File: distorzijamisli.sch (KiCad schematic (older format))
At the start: 73 parts, among them J1 SW DBG, J2 USB_OTG, J3 Conn_02x16_Odd_Even, J4 Conn_02x16_Odd_Even, J5 Conn_02x12_Odd_Even, J6 Conn_02x03_Odd_Even, J7 Conn_02x03_Odd_Even, SW1 SW_Push, U1 STM32F407VGTx, X1 Crystal

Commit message: Add codec subsheet
This adds the subsheet with the CS4245 audio codec
connected to the main processor.
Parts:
- removed R16, R22: R_Small, symbol R_Small
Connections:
- net labels added: PB14, PC12
- net labels removed: I2S2_ext_SD, I2S3_ext_SD
- wire segments 372 -> 345
- no-connect marks 16 -> 9

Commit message: Add power regulators with 5, 3 and 3.3V.
In addition, the connector is now as short as needed.
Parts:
- removed J5: Conn_02x12_Odd_Even, symbol Conn_02x12_Odd_Even
- added C55, C58, C60, C63, C65: 1uF, symbol C
- added C56, C59, C61, C64, C66: 100nF, symbol C
- added C57, C62: 10nF, symbol C
- added J12: 5V, symbol Jack-DC
- added J5: Conn_02x08_Odd_Even, symbol Conn_02x08_Odd_Even
- added U3: LD3985M30R_SOT23, TO_SOT_Packages_SMD:SOT-23-5, symbol LD3985M30R_SOT23
- added U4: LD3985M33R_SOT23, TO_SOT_Packages_SMD:SOT-23-5, symbol LD3985M33R_SOT23
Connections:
- net labels added: 3.3V, 3V, 5V
- net labels removed: VCC
- wire segments 345 -> 368
- no-connect marks 9 -> 5

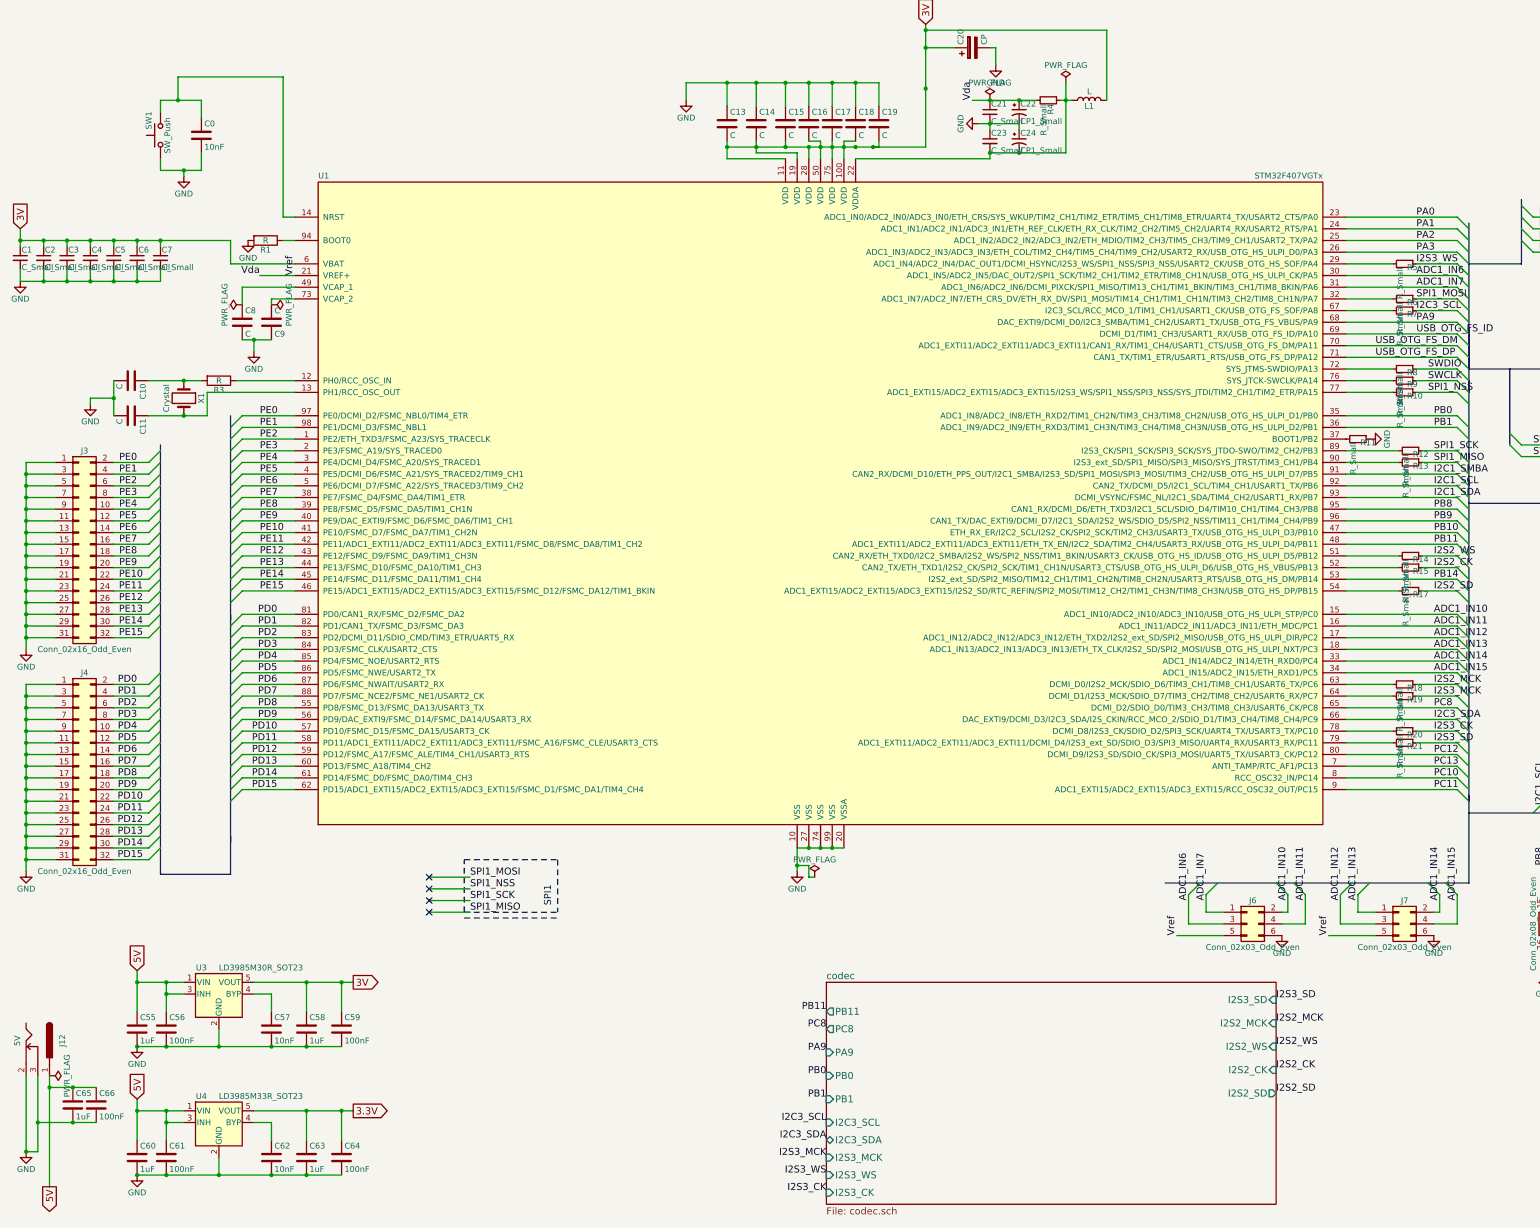
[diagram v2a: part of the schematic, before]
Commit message: Move the I2S2_SD termination resistor to driver
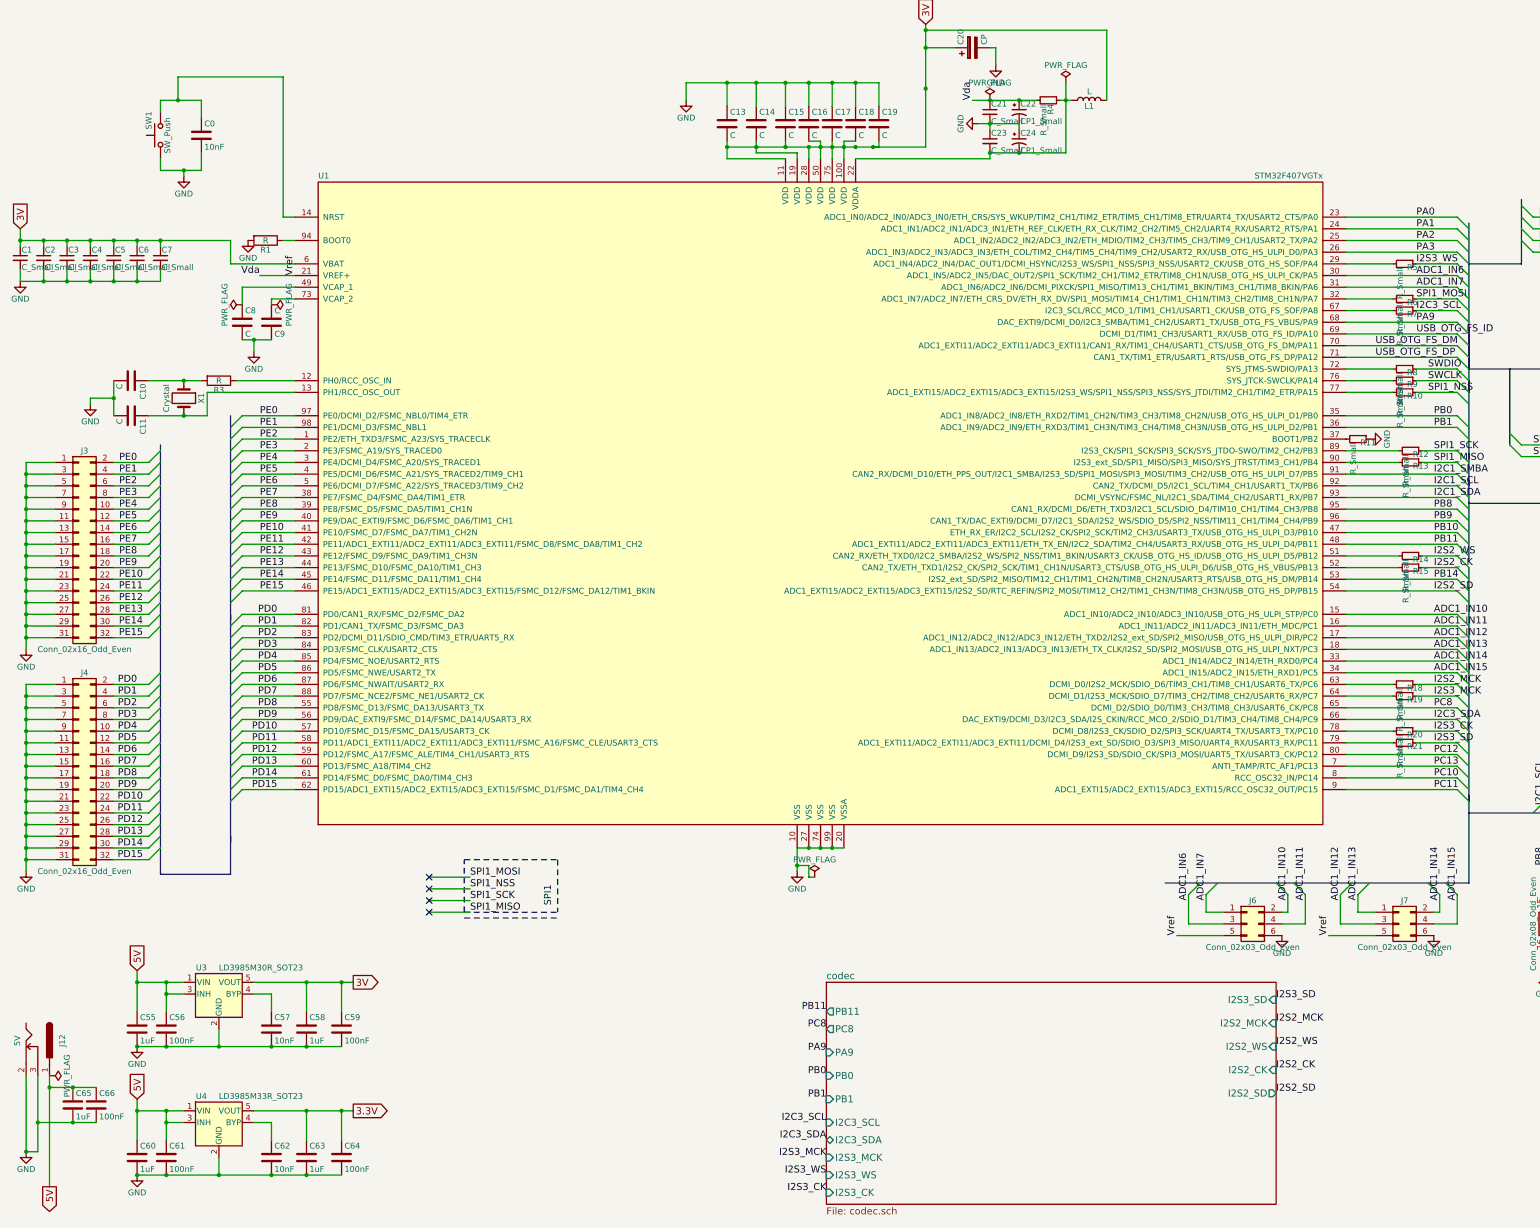
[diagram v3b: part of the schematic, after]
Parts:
- removed R17: R_Small, symbol R_Small
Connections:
- net I2S2_SD: now also U1.54 (ADC1_EXTI15/ADC2_EXTI15/ADC3_EXTI15/I2S2_SD/RTC_REFIN/SPI2_MOSI/TIM12_CH2/TIM1_CH3N/TIM8_CH3N/USB_OTG_HS_DP/PB15)

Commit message: Set values to components and minor fixes.
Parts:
- removed C20: CP, symbol CP
- added C20: 1uF, symbol C
- added R16, R2: 0, symbol R
- added R17: 100k, symbol R
- added R22: 220, symbol R
- C0: value 10nF -> 100nF
- C1, C2, C21, C23, C3, C4, C5, C6: value C_Small -> 100n
- C10, C11: value C -> 20pF
- C13, C14, C15, C16, C17, C18, C19: value C -> 100n
- C22, C24: value CP1_Small -> 1uF
- C7: value C_Small -> 1u
- C8, C9: value C -> 2.2u
- L1: value L -> fcm1608-0603
- R1: value R -> 100k
- R10, R11, R12, R13, R14, R15, R18, R19, R20, R21, R5, R6, R7: value R_Small -> 0
- R23, R24, R25, R26: value R_Small -> 1k
- R27: value R -> 1k5
- R28, R29, R3, R30: value R -> 0
- R31, R32, R33, R34, R35: value R_Small -> 10k
- R4: value R_Small -> 47
- R8, R9: value R_Small -> 22
- X1: value Crystal -> 8MHz
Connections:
- net 3V: now also R31.1, R32.1, R33.1, R34.1, R35.1, C20.2, R17.2, R2.2; no longer C1.1, C2.1, C3.1, C4.1, C5.1, C6.1, C7.1, U1.6 (VBAT)
- net GND: now also C24.2, C20.1; no longer C24.1
- net at C11.1, X1.2: now also R22.2; no longer U1.13 (PH1/RCC_OSC_OUT)
- net at C0.1, SW1.2, U1.14 (NRST): now also R17.1
- net at C23.2, L1.1, R4.1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: now also C24.1; no longer C24.2
- new net: R22.1, U1.13 (PH1/RCC_OSC_OUT)
- new net: R16.1, U1.6 (VBAT)
- new net: C1.1, C2.1, C3.1, C4.1, C5.1, C6.1, C7.1, R16.2, R2.1
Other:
- moved on the sheet: R3

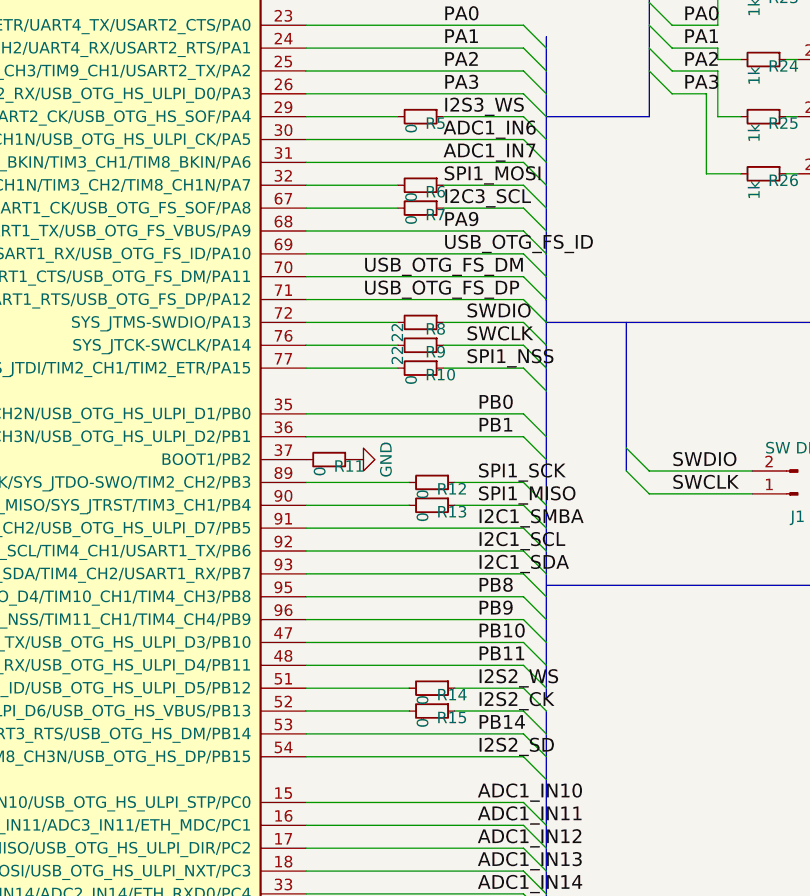
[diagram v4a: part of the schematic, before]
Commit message: Termination resistors
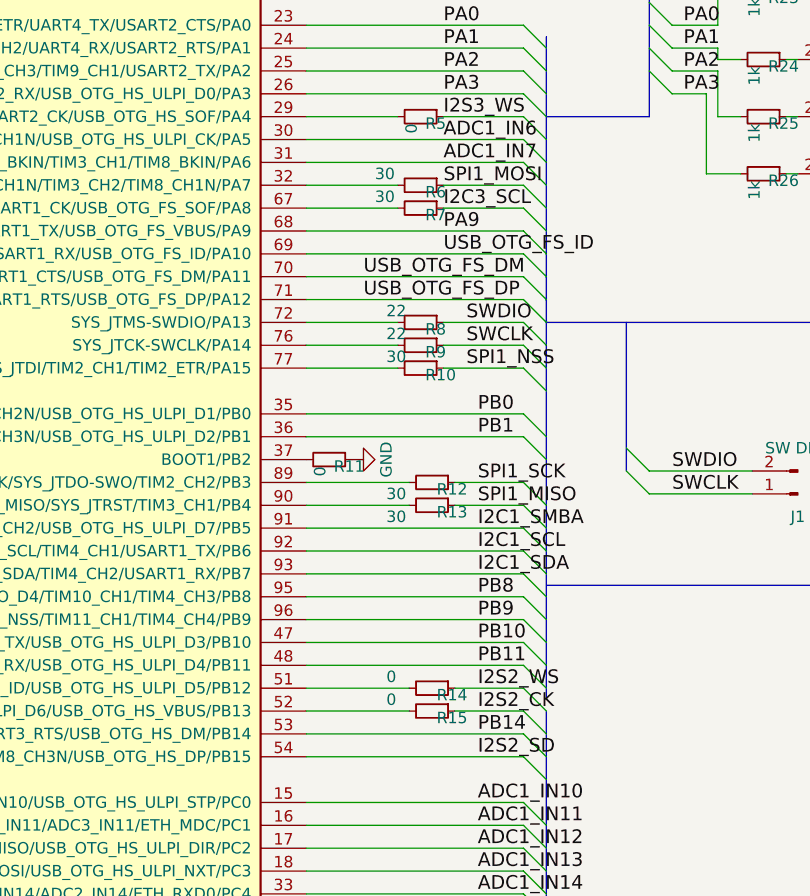
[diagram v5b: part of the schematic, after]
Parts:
- R10, R12, R13, R6, R7: value 0 -> 30
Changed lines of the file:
@@
 P 12500 3250
 F 0 "R6" V 12530 3270 50  0000 L CNN
-F 1 "0" H 12530 3210 50  0000 L CNN
+F 1 "30" V 12450 3050 50  0000 L CNN
 F 2 "" H 12500 3250 50  0001 C CNN
 F 3 "" H 12500 3250 50  0001 C CNN
@@
 P 12500 3350
 F 0 "R7" V 12530 3370 50  0000 L CNN
-F 1 "0" H 12530 3310 50  0000 L CNN
+F 1 "30" V 12450 3150 50  0000 L CNN
 F 2 "" H 12500 3350 50  0001 C CNN
 F 3 "" H 12500 3350 50  0001 C CNN
@@
 P 12500 3850
 F 0 "R8" V 12530 3870 50  0000 L CNN
-F 1 "22" H 12500 3750 50  0000 L CNN
+F 1 "22" V 12450 3700 50  0000 L CNN
 F 2 "" H 12500 3850 50  0001 C CNN
 F 3 "" H 12500 3850 50  0001 C CNN
@@
 P 12500 3950
 F 0 "R9" V 12530 3970 50  0000 L CNN
-F 1 "22" H 12500 3850 50  0000 L CNN
+F 1 "22" V 12450 3800 50  0000 L CNN
 F 2 "" H 12500 3950 50  0001 C CNN
 F 3 "" H 12500 3950 50  0001 C CNN
@@
 P 12500 4050
 F 0 "R10" V 12530 4070 50  0000 L CNN
-F 1 "0" H 12530 4010 50  0000 L CNN
+F 1 "30" V 12450 3900 50  0000 L CNN
 F 2 "" H 12500 4050 50  0001 C CNN
 F 3 "" H 12500 4050 50  0001 C CNN
@@
 P 12550 4550
 F 0 "R12" V 12580 4570 50  0000 L CNN
-F 1 "0" H 12580 4510 50  0000 L CNN
+F 1 "30" V 12600 4350 50  0000 L CNN
 F 2 "" H 12550 4550 50  0001 C CNN
 F 3 "" H 12550 4550 50  0001 C CNN
@@
 P 12550 4650
 F 0 "R13" V 12580 4670 50  0000 L CNN
-F 1 "0" H 12580 4610 50  0000 L CNN
+F 1 "30" V 12600 4450 50  0000 L CNN
 F 2 "" H 12550 4650 50  0001 C CNN
 F 3 "" H 12550 4650 50  0001 C CNN
@@
 P 12550 5450
 F 0 "R14" V 12580 5470 50  0000 L CNN
-F 1 "0" H 12580 5410 50  0000 L CNN
+F 1 "0" V 12500 5250 50  0000 L CNN
 F 2 "" H 12550 5450 50  0001 C CNN
 F 3 "" H 12550 5450 50  0001 C CNN
@@
 P 12550 5550
 F 0 "R15" V 12580 5570 50  0000 L CNN
-F 1 "0" H 12580 5510 50  0000 L CNN
+F 1 "0" V 12500 5350 50  0000 L CNN
 F 2 "" H 12550 5550 50  0001 C CNN
 F 3 "" H 12550 5550 50  0001 C CNN

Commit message: Add some of the pinouts
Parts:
- C0, L1: footprint (none) -> Inductors_SMD:L_0603_HandSoldering
- J1: footprint (none) -> Pin_Headers:Pin_Header_Straight_1x02
- J12: footprint (none) -> Connectors:BARREL_JACK
- J2: footprint (none) -> Connectors:USB_Mini-B
- J3, J4: footprint (none) -> Pin_Headers:Pin_Header_Straight_2x16
- J5: footprint (none) -> Pin_Headers:Pin_Header_Straight_2x08
- J6, J7: footprint (none) -> Pin_Headers:Pin_Header_Straight_2x03
- SW1: footprint (none) -> Buttons_Switches_THT:SW_PUSH_6mm
- U1: footprint LQFP100 -> Housings_QFP:LQFP-100_14x14mm_Pitch0.5mm
- U3, U4: footprint TO_SOT_Packages_SMD:SOT-23-5 -> TO_SOT_Packages_SMD:SOT-23-5_HandSoldering
- X1: footprint (none) -> Crystals:HC-49V
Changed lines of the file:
@@
 F 0 "C0" H 2225 1950 50  0000 L CNN
 F 1 "100nF" H 2225 1750 50  0000 L CNN
-F 2 "" H 2238 1700 50  0001 C CNN
+F 2 "Inductors_SMD:L_0603_HandSoldering" H 2238 1700 50  0001 C CNN
 F 3 "" H 2200 1850 50  0001 C CNN
 	1    2200 1850
@@
 F 0 "SW1" H 1900 1950 50  0000 L CNN
 F 1 "SW_Push" H 1850 1790 50  0000 C CNN
-F 2 "" H 1850 2050 50  0001 C CNN
+F 2 "Buttons_Switches_THT:SW_PUSH_6mm" H 1850 2050 50  0001 C CNN
 F 3 "" H 1850 2050 50  0001 C CNN
 	1    1850 1850
@@
 F 0 "J1" H 14150 4700 50  0000 C CNN
 F 1 "SW DBG" H 14150 4400 50  0000 C CNN
-F 2 "" H 14150 4600 50  0001 C CNN
+F 2 "Pin_Headers:Pin_Header_Straight_1x02" H 14150 4600 50  0001 C CNN
 F 3 "" H 14150 4600 50  0001 C CNN
 	1    14150 4600
@@
 F 0 "X1" H 2050 4250 50  0000 C CNN
 F 1 "8MHz" H 2050 3950 50  0000 C CNN
-F 2 "" H 2050 4100 50  0001 C CNN
-F 3 "" H 2050 4100 50  0001 C CNN
+F 2 "Crystals:HC-49V" H 2050 4100 50  0001 C CNN
+F 3 "CX49GFNB08000H0PESZZ" H 2050 4100 50  0001 C CNN
 	1    2050 4100
 	0    1    1    0
@@
 F 0 "J2" H 15450 4500 50  0000 L CNN
 F 1 "USB_OTG" H 15450 4400 50  0000 L CNN
-F 2 "" H 15800 4000 50  0001 C CNN
+F 2 "Connectors:USB_Mini-B" H 15800 4000 50  0001 C CNN
 F 3 "" H 15800 4000 50  0001 C CNN
 	1    15650 4050
@@
 F 0 "U1" H 3200 7875 50  0000 L BNN
 F 1 "STM32F407VGTx" H 11800 7875 50  0000 R BNN
-F 2 "LQFP100" H 11800 7825 50  0001 R TNN
+F 2 "Housings_QFP:LQFP-100_14x14mm_Pitch0.5mm" H 11800 7825 50  0001 R TNN
 F 3 "" H 7500 5050 50  0001 C CNN
 	1    7500 5050
@@
 F 0 "L1" V 9750 1550 50  0000 C CNN
 F 1 "fcm1608-0603" V 9875 1550 50  0000 C CNN
-F 2 "" H 9800 1550 50  0001 C CNN
+F 2 "Inductors_SMD:L_0603_HandSoldering" H 9800 1550 50  0001 C CNN
 F 3 "" H 9800 1550 50  0001 C CNN
 	1    9800 1550
@@
 F 0 "J3" H 1200 6150 50  0000 C CNN
 F 1 "Conn_02x16_Odd_Even" H 1200 4450 50  0000 C CNN
-F 2 "" H 1150 5350 50  0001 C CNN
+F 2 "Pin_Headers:Pin_Header_Straight_2x16" H 1150 5350 50  0001 C CNN
 F 3 "" H 1150 5350 50  0001 C CNN
 	1    1150 5350
@@
 F 0 "J4" H 1200 8050 50  0000 C CNN
 F 1 "Conn_02x16_Odd_Even" H 1200 6350 50  0000 C CNN
-F 2 "" H 1150 7250 50  0001 C CNN
+F 2 "Pin_Headers:Pin_Header_Straight_2x16" H 1150 7250 50  0001 C CNN
 F 3 "" H 1150 7250 50  0001 C CNN
 	1    1150 7250
@@
 F 0 "J6" H 11200 8800 50  0000 C CNN
 F 1 "Conn_02x03_Odd_Even" H 11200 8400 50  0000 C CNN
-F 2 "" H 11150 8600 50  0001 C CNN
+F 2 "Pin_Headers:Pin_Header_Straight_2x03" H 11150 8600 50  0001 C CNN
 F 3 "" H 11150 8600 50  0001 C CNN
 	1    11150 8600
@@
 F 0 "J7" H 12500 8800 50  0000 C CNN
 F 1 "Conn_02x03_Odd_Even" H 12500 8400 50  0000 C CNN
-F 2 "" H 12450 8600 50  0001 C CNN
+F 2 "Pin_Headers:Pin_Header_Straight_2x03" H 12450 8600 50  0001 C CNN
 F 3 "" H 12450 8600 50  0001 C CNN
 	1    12450 8600
@@
 F 0 "U3" H 2200 9425 50  0000 C CNN
 F 1 "LD3985M30R_SOT23" H 2350 9425 50  0000 L CNN
-F 2 "TO_SOT_Packages_SMD:SOT-23-5" H 2350 9525 50  0001 C CIN
+F 2 "TO_SOT_Packages_SMD:SOT-23-5_HandSoldering" H 2350 9525 50  0001 C CIN
 F 3 "" H 2350 9200 50  0001 C CNN
 	1    2350 9200
@@
 F 0 "U4" H 2200 10525 50  0000 C CNN
 F 1 "LD3985M33R_SOT23" H 2350 10525 50  0000 L CNN
-F 2 "TO_SOT_Packages_SMD:SOT-23-5" H 2350 10625 50  0001 C CIN
+F 2 "TO_SOT_Packages_SMD:SOT-23-5_HandSoldering" H 2350 10625 50  0001 C CIN
 F 3 "" H 2350 10300 50  0001 C CNN
 	1    2350 10300
@@
 F 0 "J12" H 800 9810 50  0000 C CNN
 F 1 "5V" H 800 9425 50  0000 C CNN
-F 2 "" H 850 9560 50  0001 C CNN
+F 2 "Connectors:BARREL_JACK" H 850 9560 50  0001 C CNN
 F 3 "" H 850 9560 50  0001 C CNN
 	1    800  9600
@@
 F 0 "J5" H 14150 8950 50  0000 C CNN
 F 1 "Conn_02x08_Odd_Even" H 14150 8050 50  0000 C CNN
-F 2 "" H 14100 8550 50  0001 C CNN
+F 2 "Pin_Headers:Pin_Header_Straight_2x08" H 14100 8550 50  0001 C CNN
 F 3 "" H 14100 8550 50  0001 C CNN
 	1    14100 8550
@@
 	8950 2050 8950 2000
 Wire Wire Line
-	9600 2000 8950 2000
-Wire Wire Line
-	9600 1400 9600 2000
+	8950 2000 9600 2000
+Wire Wire Line
+	9600 2000 9600 1400
 Connection ~ 9200 2000
 Connection ~ 9600 1550
@@
 	700  9900 700  10550
 Wire Wire Line
-	800  10550 700  10550
-Wire Wire Line
-	800  9900 800  10550
+	700  10550 800  10550
+Wire Wire Line
+	800  10550 800  9900
 Connection ~ 700  10550
 Wire Wire Line

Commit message: Add remaining footprints
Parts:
- C0: footprint Inductors_SMD:L_0603_HandSoldering -> Capacitors_SMD:C_0805_HandSoldering
- C1, C10, C11, C13, C14, C15, C16, C17, C18, C19, C2, C20, C21, C22, C23, C24, C3, C4, C5, C55, C56, C57, C58, C59, C6, C60, C61, C62, C63, C64, C65, C66, C7, C8, C9: footprint (none) -> Capacitors_SMD:C_0805_HandSoldering
- D1, D2, D3, D4: footprint (none) -> LEDs:LED_0805_HandSoldering
- R1, R10, R11, R12, R13, R14, R15, R16, R17, R18, R19, R2, R20, R21, R22, R23, R24, R25, R26, R27, R28, R29, R3, R30, R31, R32, R33, R34, R35, R4, R5, R6, R7, R8, R9: footprint (none) -> Resistors_SMD:R_0805_HandSoldering
